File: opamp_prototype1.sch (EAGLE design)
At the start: 18 parts, among them IC1 OPA2132P, IC2 OPA2132U

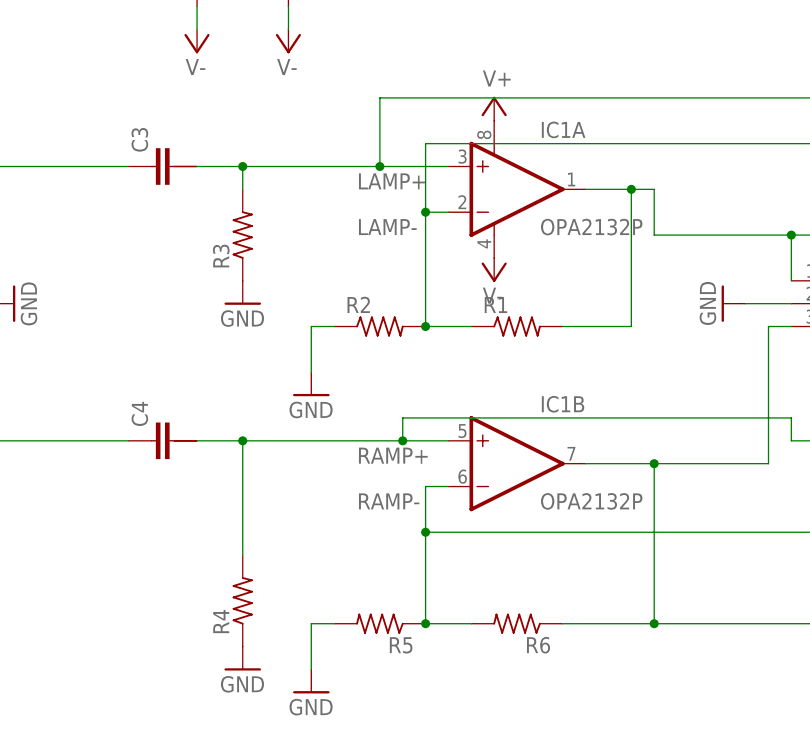
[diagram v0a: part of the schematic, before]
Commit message: Added SMD resistor option
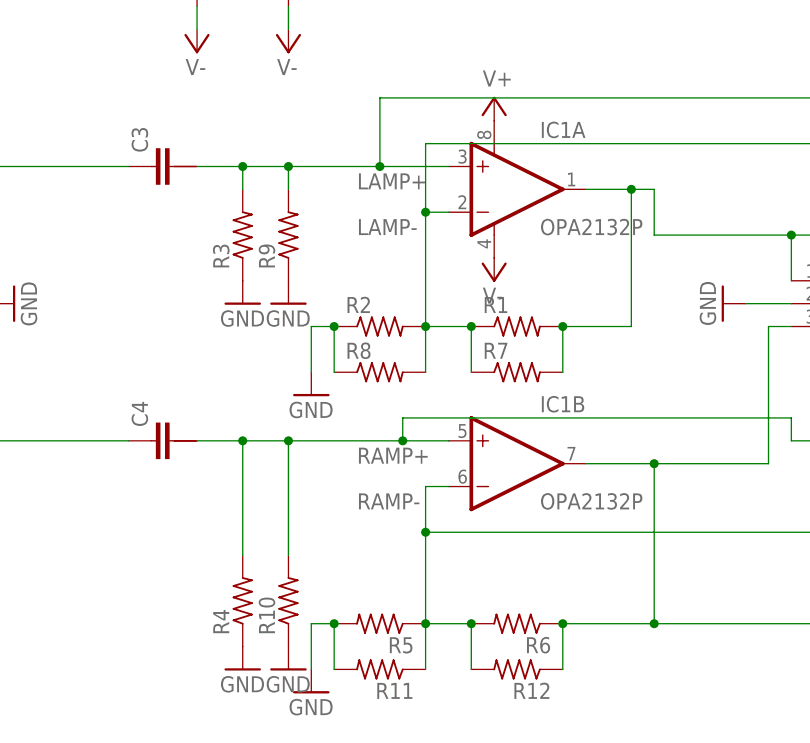
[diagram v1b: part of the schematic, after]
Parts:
- added R10, R11, R12, R7, R8, R9: (no value), rcl:R-US_R1206
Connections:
- net GND: now also R10.1, R11.2, R8.1, R9.1
- net LAMP+: now also R9.2
- net LAMP-: now also R7.1, R8.2
- net OUT_L: now also R7.2
- net OUT_R: now also R12.1
- net RAMP+: now also R10.2
- net RAMP-: now also R11.1, R12.2
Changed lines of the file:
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@@
 <part name="OUT" library="SparkFun-Connectors" deviceset="M03" device="PTH"/>
 <part name="GND12" library="supply1" deviceset="GND" device=""/>
+<part name="R7" library="rcl" deviceset="R-US_" device="R1206"/>
+<part name="R8" library="rcl" deviceset="R-US_" device="R1206"/>
+<part name="R9" library="rcl" deviceset="R-US_" device="R1206"/>
+<part name="R10" library="rcl" deviceset="R-US_" device="R1206"/>
+<part name="R11" library="rcl" deviceset="R-US_" device="R1206"/>
+<part name="R12" library="rcl" deviceset="R-US_" device="R1206"/>
+<part name="GND11" library="supply1" deviceset="GND" device=""/>
+<part name="GND13" library="supply1" deviceset="GND" device=""/>
 </parts>
 <sheets>
@@
 <instance part="OUT" gate="J$1" x="91.44" y="43.18" rot="R180"/>
 <instance part="GND12" gate="1" x="76.2" y="43.18" rot="R270"/>
+<instance part="R7" gate="G$1" x="53.34" y="35.56"/>
+<instance part="R8" gate="G$1" x="38.1" y="35.56"/>
+<instance part="R9" gate="G$1" x="27.94" y="50.8" rot="R90"/>
+<instance part="R10" gate="G$1" x="27.94" y="10.16" rot="R90"/>
+<instance part="R11" gate="G$1" x="38.1" y="2.54" rot="R180"/>
+<instance part="R12" gate="G$1" x="53.34" y="2.54" rot="R180"/>
+<instance part="GND11" gate="1" x="27.94" y="43.18"/>
+<instance part="GND13" gate="1" x="27.94" y="2.54"/>
 </instances>
 <busses>
@@
 <pinref part="GND7" gate="1" pin="GND"/>
 <wire x1="30.48" y1="40.64" x2="30.48" y2="35.56" width="0.1524" layer="91"/>
+<pinref part="R8" gate="G$1" pin="1"/>
+<wire x1="33.02" y1="35.56" x2="33.02" y2="40.64" width="0.1524" layer="91"/>
+<junction x="33.02" y="40.64"/>
 </segment>
 <segment>
@@
 <pinref part="GND6" gate="1" pin="GND"/>
 <wire x1="30.48" y1="7.62" x2="30.48" y2="2.54" width="0.1524" layer="91"/>
+<pinref part="R11" gate="G$1" pin="2"/>
+<wire x1="33.02" y1="2.54" x2="33.02" y2="7.62" width="0.1524" layer="91"/>
+<junction x="33.02" y="7.62"/>
 </segment>
 <segment>
@@
 <wire x1="83.82" y1="43.18" x2="78.74" y2="43.18" width="0.1524" layer="91"/>
 </segment>
+<segment>
+<pinref part="R9" gate="G$1" pin="1"/>
+<pinref part="GND11" gate="1" pin="GND"/>
+</segment>
+<segment>
+<pinref part="R10" gate="G$1" pin="1"/>
+<pinref part="GND13" gate="1" pin="GND"/>
+</segment>
 </net>
 <net name="LAMP+" class="0">
@@
 <wire x1="17.78" y1="58.42" x2="22.86" y2="58.42" width="0.1524" layer="91"/>
 <pinref part="R3" gate="G$1" pin="2"/>
-<wire x1="22.86" y1="58.42" x2="38.1" y2="58.42" width="0.1524" layer="91"/>
+<wire x1="22.86" y1="58.42" x2="27.94" y2="58.42" width="0.1524" layer="91"/>
+<wire x1="27.94" y1="58.42" x2="38.1" y2="58.42" width="0.1524" layer="91"/>
 <wire x1="38.1" y1="58.42" x2="45.72" y2="58.42" width="0.1524" layer="91"/>
 <wire x1="22.86" y1="58.42" x2="22.86" y2="55.88" width="0.1524" layer="91"/>
@@
 <junction x="38.1" y="58.42"/>
 <label x="35.56" y="55.88" size="1.778" layer="95"/>
+<pinref part="R9" gate="G$1" pin="2"/>
+<wire x1="27.94" y1="55.88" x2="27.94" y2="58.42" width="0.1524" layer="91"/>
+<junction x="27.94" y="58.42"/>
 </segment>
 </net>
@@
 <wire x1="17.78" y1="27.94" x2="22.86" y2="27.94" width="0.1524" layer="91"/>
 <pinref part="R4" gate="G$1" pin="2"/>
-<wire x1="22.86" y1="27.94" x2="40.64" y2="27.94" width="0.1524" layer="91"/>
+<wire x1="22.86" y1="27.94" x2="27.94" y2="27.94" width="0.1524" layer="91"/>
+<wire x1="27.94" y1="27.94" x2="40.64" y2="27.94" width="0.1524" layer="91"/>
 <wire x1="40.64" y1="27.94" x2="45.72" y2="27.94" width="0.1524" layer="91"/>
 <wire x1="22.86" y1="27.94" x2="22.86" y2="15.24" width="0.1524" layer="91"/>
@@
 <junction x="40.64" y="27.94"/>
 <label x="35.56" y="25.4" size="1.778" layer="95"/>
+<pinref part="R10" gate="G$1" pin="2"/>
+<wire x1="27.94" y1="15.24" x2="27.94" y2="27.94" width="0.1524" layer="91"/>
+<junction x="27.94" y="27.94"/>
 </segment>
 </net>
@@
 <wire x1="81.28" y1="40.64" x2="83.82" y2="40.64" width="0.1524" layer="91"/>
 <junction x="68.58" y="25.4"/>
+<pinref part="R12" gate="G$1" pin="1"/>
+<wire x1="58.42" y1="2.54" x2="58.42" y2="7.62" width="0.1524" layer="91"/>
+<junction x="58.42" y="7.62"/>
 </segment>
 </net>
@@
 <junction x="43.18" y="17.78"/>
 <label x="35.56" y="20.32" size="1.778" layer="95"/>
+<pinref part="R11" gate="G$1" pin="1"/>
+<wire x1="43.18" y1="2.54" x2="43.18" y2="7.62" width="0.1524" layer="91"/>
+<pinref part="R12" gate="G$1" pin="2"/>
+<wire x1="48.26" y1="2.54" x2="48.26" y2="7.62" width="0.1524" layer="91"/>
+<junction x="48.26" y="7.62"/>
 </segment>
 </net>
@@
 <wire x1="83.82" y1="45.72" x2="83.82" y2="50.8" width="0.1524" layer="91"/>
 <junction x="83.82" y="50.8"/>
+<pinref part="R7" gate="G$1" pin="2"/>
+<wire x1="58.42" y1="35.56" x2="58.42" y2="40.64" width="0.1524" layer="91"/>
+<junction x="58.42" y="40.64"/>
 </segment>
 </net>
@@
 <junction x="43.18" y="53.34"/>
 <label x="35.56" y="50.8" size="1.778" layer="95"/>
-</segment>
-</net>
+<pinref part="R7" gate="G$1" pin="1"/>
+<wire x1="48.26" y1="35.56" x2="48.26" y2="40.64" width="0.1524" layer="91"/>
+<pinref part="R8" gate="G$1" pin="2"/>
+<wire x1="43.18" y1="35.56" x2="43.18" y2="40.64" width="0.1524" layer="91"/>
+<junction x="48.26" y="40.64"/>
+</segment>
+</net>
